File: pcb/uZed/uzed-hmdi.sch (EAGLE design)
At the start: 6 parts, among them U11 PCA9306

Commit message: hdmi connections copied in from scarab hardware board
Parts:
- removed U$3, U$4: HDMI-A, new-connectors:HDMI-A
- removed U11: PCA9306, saanlima:PCA9306
- added C1, C39: .1uF, rcl:C-EUC0603K
- added J5, J6: HDMI-TYPE-A-RECEPTICALFCI10029449, saanlima:HDMI-TYPE-A-RECEPTICALFCI10029449
- added PCA9306: PCA9306, saanlima:PCA9306
- added R1, R2: 100K, rcl:R-US_R0603
- added R3: 0, rcl:R-US_R0603
- added R4, R5: 10K, rcl:R-US_R0603
- added RN1, RN2: 2k, resistor-dil:2R-NEXB34V
- added RN3, RN4, RN5, RN6: 51, resistor-dil:2R-NEXB34V
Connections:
- new net 3V3: PCA9306.VREF1, R3.2, RN1A.2, RN1B.2
- new net GND: C1.2, C39.2, J5.CLOCKSHIELD, J5.DATA0SHIELD, J5.DATA1SHIELD, J5.DATA2SHIELD, J5.DDC/CEC-GRND, J5.RES, J6.CLOCKSHIELD, J6.DATA0SHIELD, J6.DATA1SHIELD, J6.DATA2SHIELD, J6.DDC/CEC-GRND, J6.RES, PCA9306.GND, R1.1, R2.1, R4.1
- new net N$1: C1.1, J5.SH1, J5.SH2, J5.SH3, J5.SH4, R1.2
- new net N$10: J5.DETECT, R4.2
- new net N$11: R3.1, RN3A.2, RN3B.2, RN4A.2, RN4B.2, RN5A.2, RN5B.2, RN6A.2, RN6B.2
- new net N$12: J6.DETECT, R5.1
- new net N$13: J6.+5V, PCA9306.EN, PCA9306.VREF2, R5.2, RN2A.2, RN2B.2
- new net N$15: J6.SDA, PCA9306.SDA2, RN2B.1
- new net N$16: J6.SCL, PCA9306.SCL2, RN2A.1
- new net N$17: PCA9306.SCL1, RN1A.1
- new net N$18: PCA9306.SDA1, RN1B.1
- new net N$19: J5.DATA2+
- new net N$2: J6.DATA2+, RN6B.1
- new net N$20: J5.DATA2-
- new net N$21: J5.DATA1+
- new net N$22: J5.DATA1-
- new net N$23: J5.DATA0+
- new net N$24: J5.DATA0-
- new net N$25: J5.CLOCK+
- new net N$26: J5.CLOCK-
- new net N$3: J6.DATA2-, RN6A.1
- new net N$34: C39.1, J6.SH1, J6.SH2, J6.SH3, J6.SH4, R2.2
- new net N$4: J6.DATA1+, RN5B.1
- new net N$5: J6.DATA1-, RN5A.1
- new net N$6: J6.DATA0+, RN4B.1
- new net N$7: J6.DATA0-, RN4A.1
- new net N$8: J6.CLOCK+, RN3B.1
- new net N$9: J6.CLOCK-, RN3A.1

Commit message: hdmi added in from scarab board
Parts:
- removed RN1, RN2: 2k, resistor-dil:2R-NEXB34V
- added RN7: 2k, resistor-dil:4R-N0603-ARV
- renumbered U$1 to JX2, U$2 to JX1
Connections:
- net 3V3: now also RN7A.1, RN7B.1; no longer RN1A.2, RN1B.2
- net N$13: now also RN7C.1, RN7D.1; no longer RN2A.2, RN2B.2
- net N$15: now also RN7C.2; no longer RN2B.1
- net N$16: now also RN7D.2; no longer RN2A.1
- net N$17: now also RN7B.2; no longer RN1A.1
- net N$18: now also RN7A.2; no longer RN1B.1
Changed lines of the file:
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@@
 </classes>
 <parts>
-<part name="U$1" library="lupa300-components" deviceset="BERGSTAK-100POS" device=""/>
-<part name="U$2" library="lupa300-components" deviceset="BERGSTAK-100POS" device=""/>
+<part name="JX2" library="lupa300-components" deviceset="BERGSTAK-100POS" device=""/>
+<part name="JX1" library="lupa300-components" deviceset="BERGSTAK-100POS" device=""/>
 <part name="U$5" library="lupa300-components" deviceset="SI514" device=""/>
 <part name="RN3" library="resistor-dil" library_urn="urn:adsk.eagle:library:342" deviceset="2R-N" device="EXB34V" package3d_urn="urn:adsk.eagle:package:24930/1" value="51"/>
@@
 <part name="PCA9306" library="saanlima" deviceset="PCA9306" device=""/>
 <part name="GND4" library="SparkFun" deviceset="GND" device=""/>
-<part name="RN1" library="resistor-dil" library_urn="urn:adsk.eagle:library:342" deviceset="2R-N" device="EXB34V" package3d_urn="urn:adsk.eagle:package:24930/1" value="2k"/>
-<part name="RN2" library="resistor-dil" library_urn="urn:adsk.eagle:library:342" deviceset="2R-N" device="EXB34V" package3d_urn="urn:adsk.eagle:package:24930/1" value="2k"/>
+<part name="RN7" library="resistor-dil" deviceset="4R-N" device="0603-ARV" value="2k"/>
 </parts>
 <sheets>
@@
 </plain>
 <instances>
-<instance part="U$1" gate="G$1" x="-104.14" y="63.5"/>
-<instance part="U$2" gate="G$1" x="119.38" y="66.04"/>
+<instance part="JX2" gate="G$1" x="-104.14" y="63.5"/>
+<instance part="JX1" gate="G$1" x="119.38" y="66.04"/>
 <instance part="U$5" gate="G$1" x="-7.62" y="-20.32"/>
 </instances>
@@
 <instance part="PCA9306" gate="G$1" x="-30.48" y="-13.97"/>
 <instance part="GND4" gate="1" x="-49.53" y="-48.26"/>
-<instance part="RN1" gate="A" x="-80.01" y="8.89" rot="R90"/>
-<instance part="RN1" gate="B" x="-74.93" y="8.89" rot="R90"/>
-<instance part="RN2" gate="A" x="-7.62" y="8.89" rot="R90"/>
-<instance part="RN2" gate="B" x="-3.81" y="8.89" rot="R90"/>
+<instance part="RN7" gate="A" x="-74.93" y="8.89" rot="R270"/>
+<instance part="RN7" gate="B" x="-80.01" y="8.89" rot="R270"/>
+<instance part="RN7" gate="C" x="-3.81" y="8.89" rot="R270"/>
+<instance part="RN7" gate="D" x="-7.62" y="8.89" rot="R270"/>
 </instances>
 <busses>
@@
 <wire x1="-45.72" y1="-8.89" x2="-54.61" y2="-8.89" width="0.1524" layer="91"/>
 <label x="-64.77" y="-8.89" size="1.778" layer="95"/>
-<pinref part="RN1" gate="A" pin="2"/>
 <wire x1="-54.61" y1="-8.89" x2="-64.77" y2="-8.89" width="0.1524" layer="91"/>
 <wire x1="-80.01" y1="13.97" x2="-80.01" y2="16.51" width="0.1524" layer="91"/>
 <wire x1="-80.01" y1="16.51" x2="-74.93" y2="16.51" width="0.1524" layer="91"/>
-<pinref part="RN1" gate="B" pin="2"/>
 <wire x1="-74.93" y1="16.51" x2="-74.93" y2="13.97" width="0.1524" layer="91"/>
 <wire x1="-74.93" y1="16.51" x2="-54.61" y2="16.51" width="0.1524" layer="91"/>
 <wire x1="-54.61" y1="16.51" x2="-54.61" y2="-8.89" width="0.1524" layer="91"/>
 <junction x="-54.61" y="-8.89"/>
+<pinref part="RN7" gate="B" pin="1"/>
+<pinref part="RN7" gate="A" pin="1"/>
 </segment>
 </net>
@@
 <wire x1="-10.16" y1="-8.89" x2="-10.16" y2="-6.35" width="0.1524" layer="91"/>
 <junction x="-10.16" y="-6.35"/>
-<pinref part="RN2" gate="A" pin="2"/>
 <wire x1="-7.62" y1="13.97" x2="-7.62" y2="16.51" width="0.1524" layer="91"/>
 <wire x1="-7.62" y1="16.51" x2="-3.81" y2="16.51" width="0.1524" layer="91"/>
-<pinref part="RN2" gate="B" pin="2"/>
 <wire x1="-3.81" y1="13.97" x2="-3.81" y2="16.51" width="0.1524" layer="91"/>
 <wire x1="-3.81" y1="16.51" x2="2.54" y2="16.51" width="0.1524" layer="91"/>
 <wire x1="2.54" y1="16.51" x2="2.54" y2="-6.35" width="0.1524" layer="91"/>
 <junction x="2.54" y="-6.35"/>
+<pinref part="RN7" gate="D" pin="1"/>
+<pinref part="RN7" gate="C" pin="1"/>
 </segment>
 </net>
@@
 <pinref part="PCA9306" gate="G$1" pin="SDA2"/>
 <wire x1="11.43" y1="-13.97" x2="-3.81" y2="-13.97" width="0.1524" layer="91"/>
-<pinref part="RN2" gate="B" pin="1"/>
 <wire x1="-3.81" y1="-13.97" x2="-15.24" y2="-13.97" width="0.1524" layer="91"/>
 <wire x1="-3.81" y1="3.81" x2="-3.81" y2="-13.97" width="0.1524" layer="91"/>
 <junction x="-3.81" y="-13.97"/>
+<pinref part="RN7" gate="C" pin="2"/>
 </segment>
 </net>
@@
 <pinref part="PCA9306" gate="G$1" pin="SCL2"/>
 <wire x1="7.62" y1="-11.43" x2="-7.62" y2="-11.43" width="0.1524" layer="91"/>
-<pinref part="RN2" gate="A" pin="1"/>
 <wire x1="-7.62" y1="-11.43" x2="-15.24" y2="-11.43" width="0.1524" layer="91"/>
 <wire x1="-7.62" y1="3.81" x2="-7.62" y2="-11.43" width="0.1524" layer="91"/>
 <junction x="-7.62" y="-11.43"/>
+<pinref part="RN7" gate="D" pin="2"/>
 </segment>
 </net>
@@
 <pinref part="PCA9306" gate="G$1" pin="SCL1"/>
 <wire x1="-45.72" y1="-11.43" x2="-80.01" y2="-11.43" width="0.1524" layer="91"/>
-<pinref part="RN1" gate="A" pin="1"/>
 <wire x1="-80.01" y1="-11.43" x2="-86.36" y2="-11.43" width="0.1524" layer="91"/>
 <wire x1="-80.01" y1="3.81" x2="-80.01" y2="-11.43" width="0.1524" layer="91"/>
 <junction x="-80.01" y="-11.43"/>
+<pinref part="RN7" gate="B" pin="2"/>
 </segment>
 </net>
@@
 <pinref part="PCA9306" gate="G$1" pin="SDA1"/>
 <wire x1="-45.72" y1="-13.97" x2="-74.93" y2="-13.97" width="0.1524" layer="91"/>
-<pinref part="RN1" gate="B" pin="1"/>
 <wire x1="-74.93" y1="-13.97" x2="-86.36" y2="-13.97" width="0.1524" layer="91"/>
 <wire x1="-74.93" y1="3.81" x2="-74.93" y2="-13.97" width="0.1524" layer="91"/>
 <junction x="-74.93" y="-13.97"/>
-</segment>
-</net>
+<pinref part="RN7" gate="A" pin="2"/>
+</segment>
+</net>

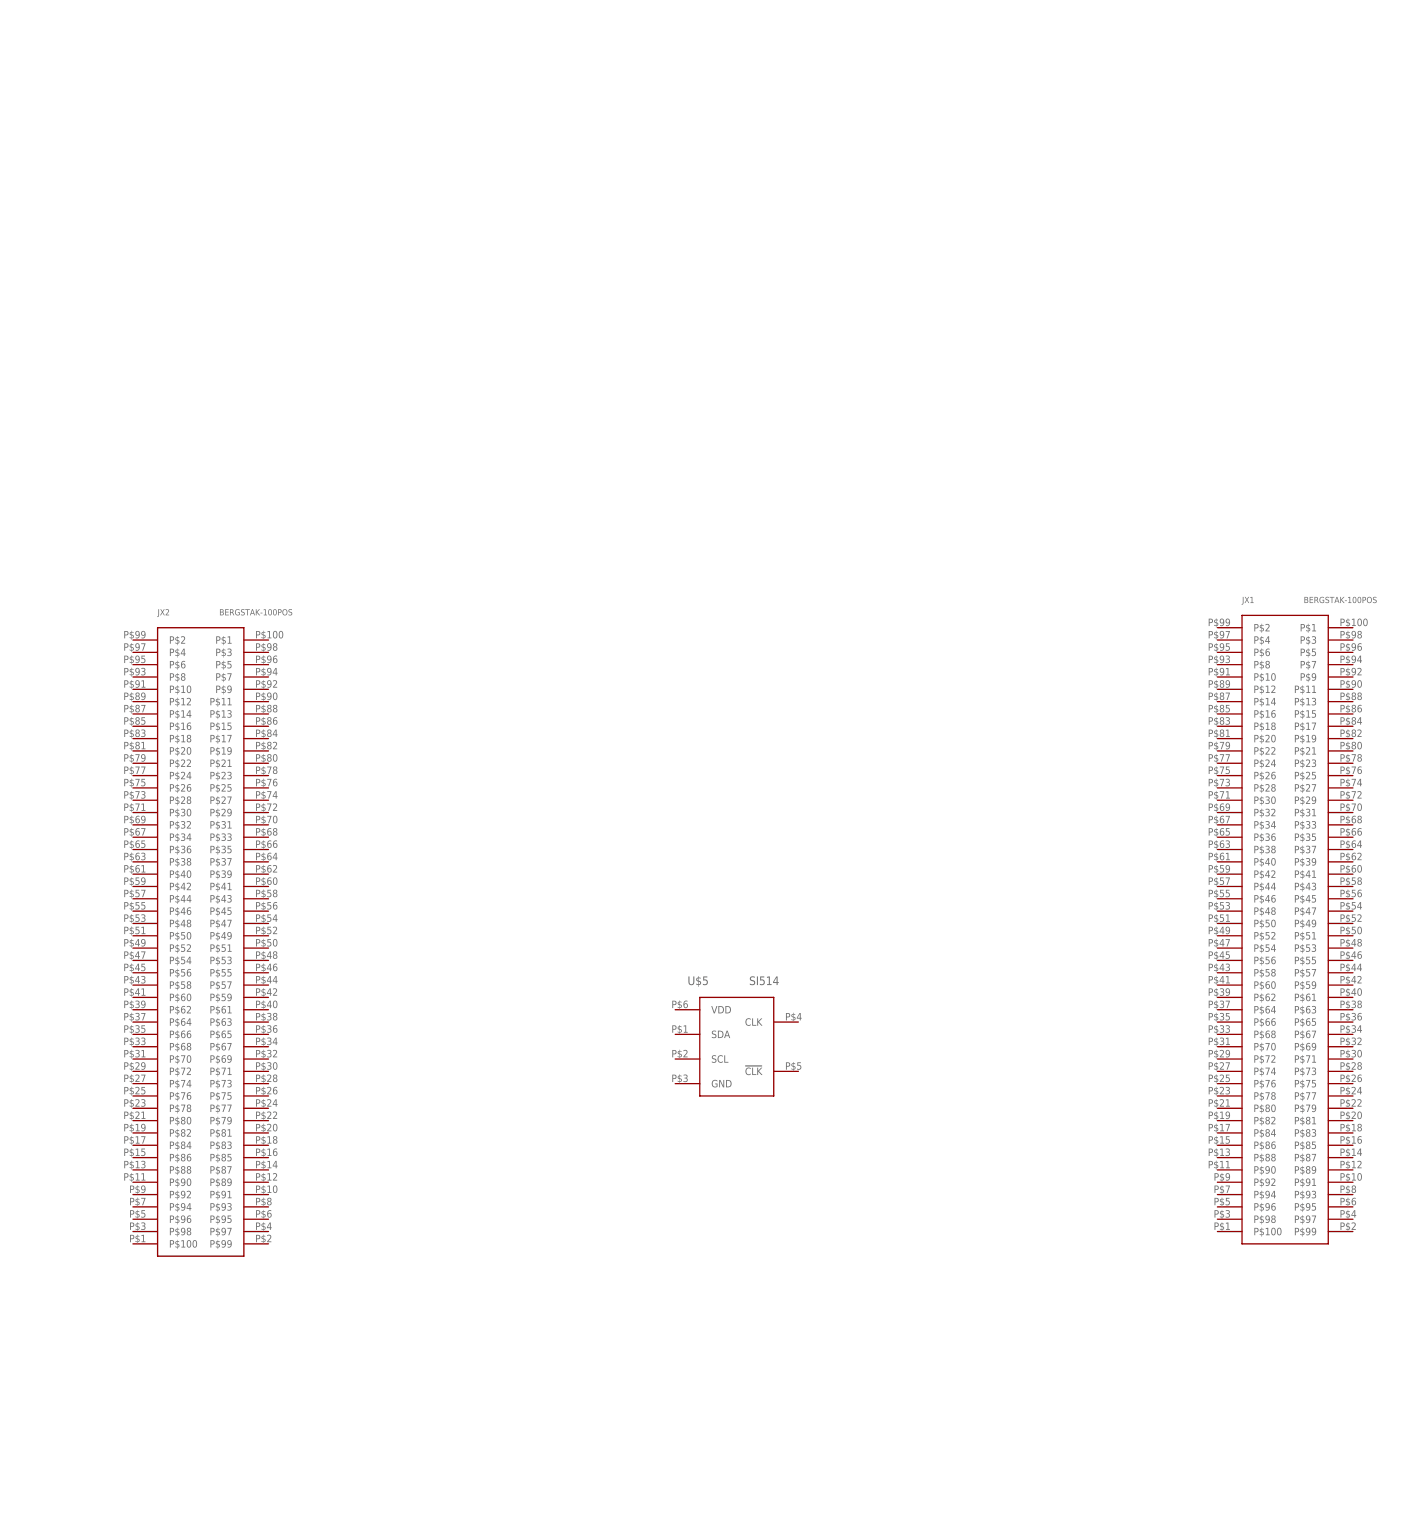
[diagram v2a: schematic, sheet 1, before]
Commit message: more work on hdmi, layout with mounting holes complete, bergstak connectors aligned to be to carrier board spec
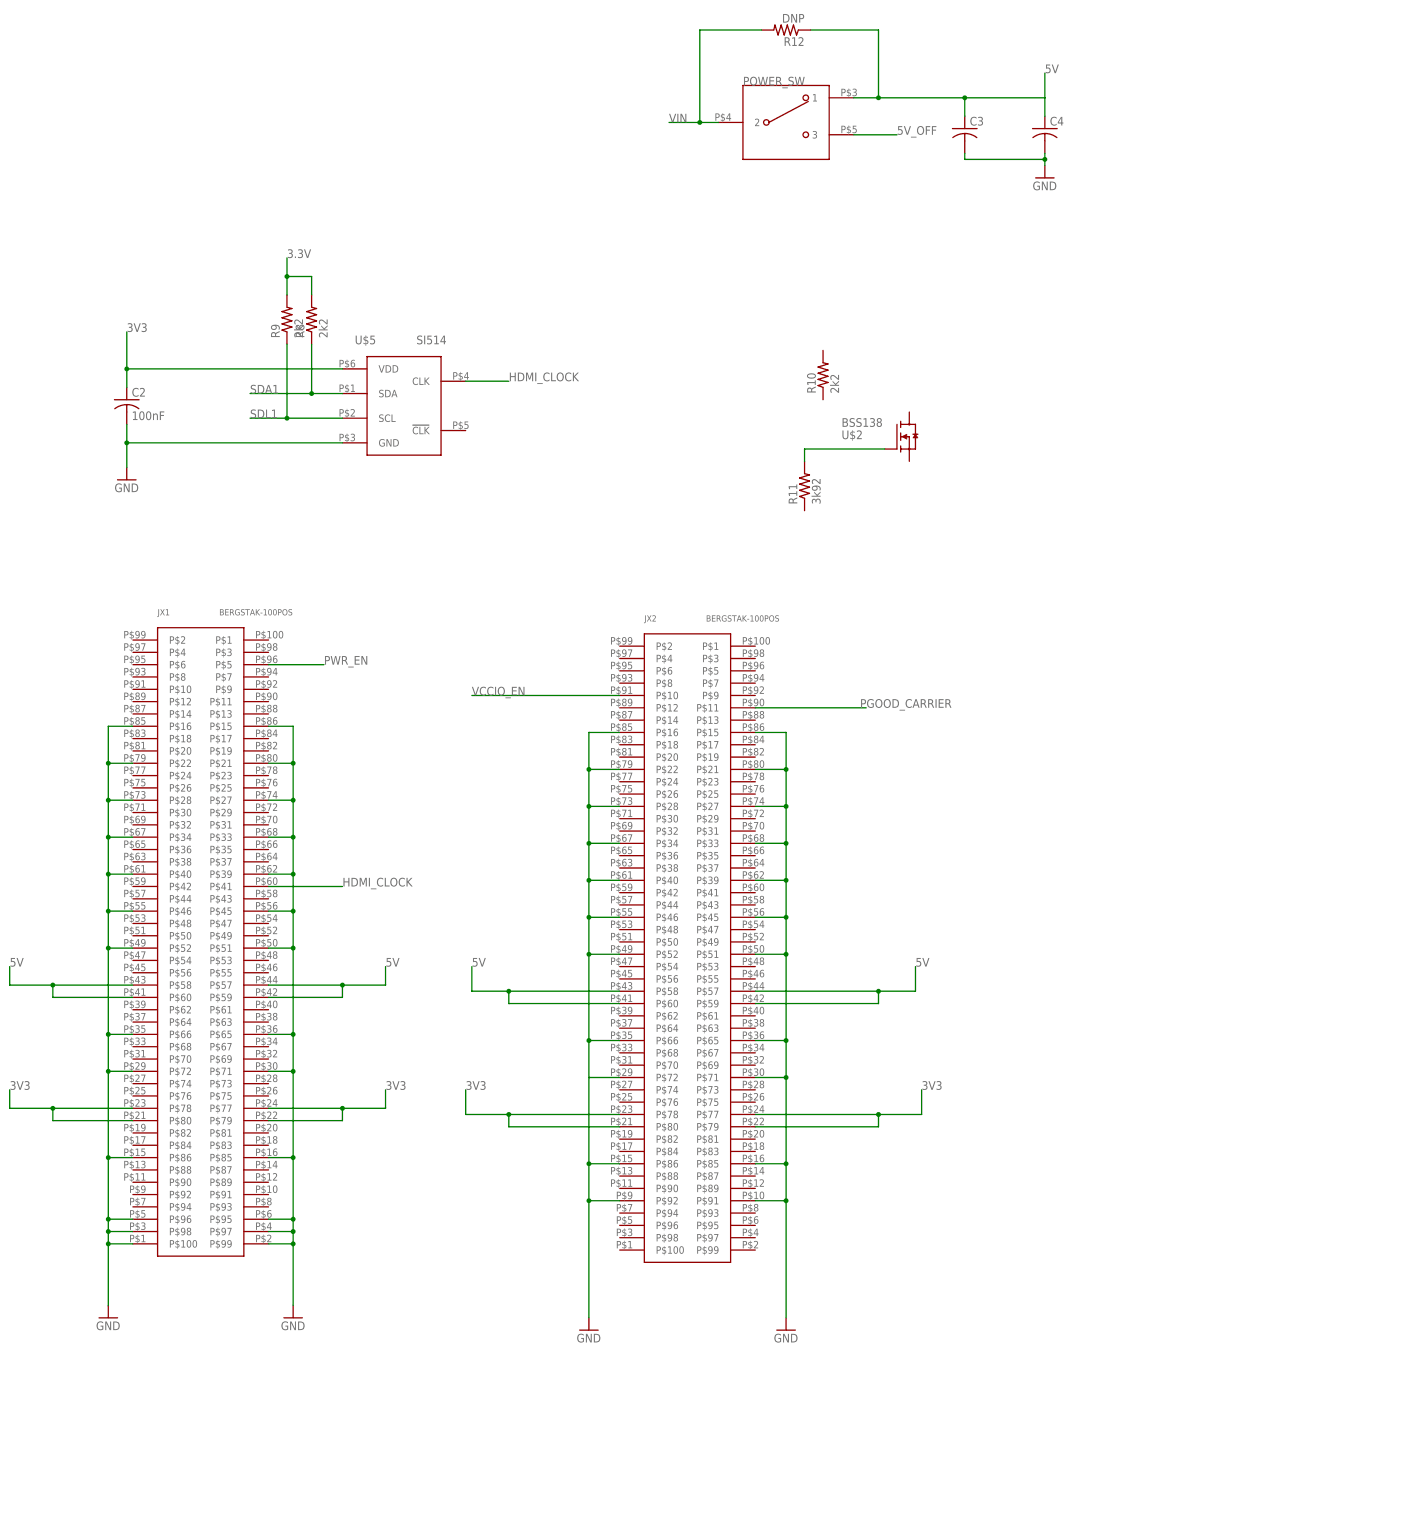
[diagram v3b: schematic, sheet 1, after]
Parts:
- added C2: 100nF, rcl:C-USC0603
- added C3: (no value), rcl:C-USC0603
- added C4: (no value), rcl:C-USC1206K
- added POWER_SW: T511006, lupa300-components:T511006
- added R10, R8, R9: 2k2, rcl:R-US_R0603
- added R11: 3k92, rcl:R-US_R0603
- added R12: DNP, rcl:R-US_R0603
- added R6: 10K, rcl:R-US_R0603
- added R7: 0, rcl:R-US_R0603
- added U$1, U$2: BSS138, lupa300-components:BSS138
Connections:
- net N$17 renamed SCL2
- net N$18 renamed SDA2
- net N$19 renamed P2_DATA2+
- net N$2 renamed P1_DATA2+
- net N$20 renamed P2_DATA2-
- net N$21 renamed P2_DATA1+
- net N$22 renamed P2_DATA1-
- net N$23 renamed P2_DATA0+
- net N$24 renamed P2_DATA0-
- net N$25 renamed P2_CLOCK+
- net N$26 renamed P2_CLOCK-
- net N$3 renamed P1_DATA2-
- net N$4 renamed P1_DATA1+
- net N$5 renamed P1_DATA1-
- net N$6 renamed P1_DATA0+
- net N$7 renamed P1_DATA0-
- net N$8 renamed P1_CLOCK+
- net N$9 renamed P1_CLOCK-
- removed net N$13: J6.+5V, PCA9306.EN, PCA9306.VREF2, R5.2, RN7C.1, RN7D.1
- new net 3.3V: R8.2, R9.2
- new net 5V: C3.1, C4.1, J6.+5V, JX1.P$57, JX1.P$58, JX1.P$59, JX1.P$60, JX2.P$57, JX2.P$58, JX2.P$59, JX2.P$60, PCA9306.EN, PCA9306.VREF2, POWER_SW.1, R12.1, R5.2, R7.1, RN7C.1, RN7D.1
- new net 5V_OFF: POWER_SW.3
- new net DET_CONTROL: R6.2, U$1.G
- new net HDMI_CLOCK: JX1.P$41, U$5.CLK
- new net N$14: J5.+5V, R7.2
- new net N$2: R11.2, U$2.G
- new net PGOOD_CARRIER: JX2.P$11
- new net PWR_EN: JX1.P$5
- new net SDA1: R8.1, U$5.SDA
- new net SDL1: R9.1, U$5.SCL
- new net VCCIO_EN: JX2.P$10
- new net VIN: POWER_SW.2, R12.2
- net 3V3: now also C2.1, JX1.P$77, JX1.P$78, JX1.P$79, JX1.P$80, JX2.P$77, JX2.P$78, JX2.P$79, JX2.P$80, R6.1, U$5.VDD
- net GND: now also C2.2, C3.2, C4.2, JX1.P$100, JX1.P$15, JX1.P$16, JX1.P$21, JX1.P$22, JX1.P$27, JX1.P$28, JX1.P$33, JX1.P$34, JX1.P$39, JX1.P$40, JX1.P$45, JX1.P$46, JX1.P$51, JX1.P$52, JX1.P$65, JX1.P$66, JX1.P$71, JX1.P$72, JX1.P$85, JX1.P$86, JX1.P$95, JX1.P$96, JX1.P$97, JX1.P$98, JX1.P$99, JX2.P$15, JX2.P$16, JX2.P$21, JX2.P$22, JX2.P$27, JX2.P$28, JX2.P$33, JX2.P$34, JX2.P$39, JX2.P$40, JX2.P$45, JX2.P$46, JX2.P$51, JX2.P$52, JX2.P$65, JX2.P$66, JX2.P$71, JX2.P$72, JX2.P$85, JX2.P$86, JX2.P$91, JX2.P$92, U$1.S, U$5.GND
- net N$12: now also U$1.D
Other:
- moved on the sheet: JX1, JX2, RN7A, RN7B, RN7C, RN7D, U$5
